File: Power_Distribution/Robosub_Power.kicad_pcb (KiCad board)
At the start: 2 copper layers, 120 x 60 mm, 47 parts, among them J1 1135333, J10 1135333, J14 Conn_01x04, J2 1135333, J3 1135333, J4 1135333, J5 1135333, J6 1135333, J7 1135333, J8 1135333, J9 1135333, U1 INA300AIDSQT, U2 SN74LVC1G97DBVR, U3 AUIR3241STR, U4 BSC0702LSATMA1, U5 BSC0702LSATMA1, U6 BSC0702LSATMA1, U7 NVTR01P02LT1G, U8 NVTR01P02LT1G

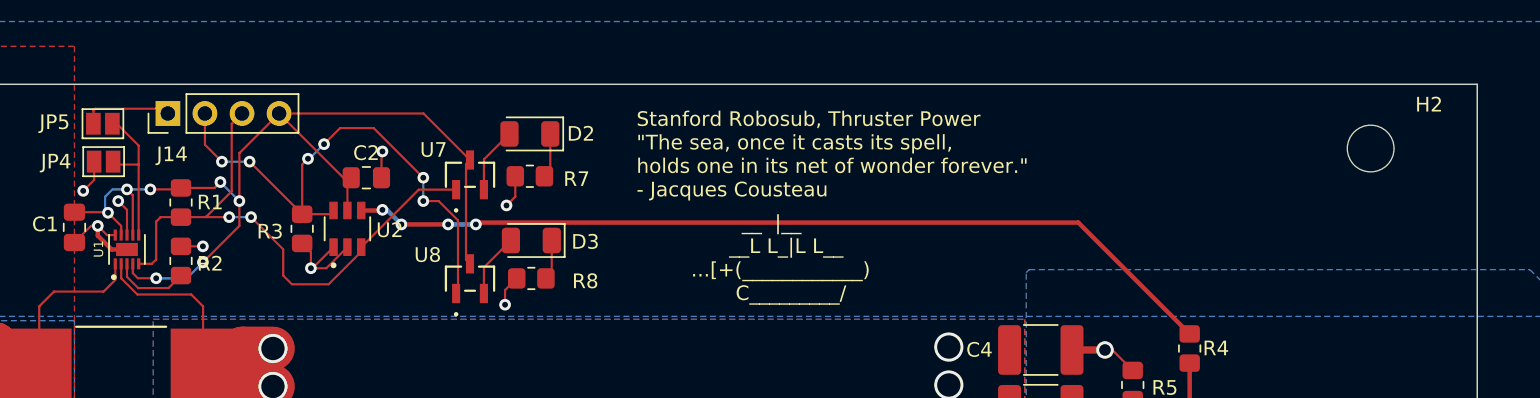
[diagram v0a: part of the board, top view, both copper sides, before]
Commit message: power rev2[fix diodes, ground loop, silkscreen]
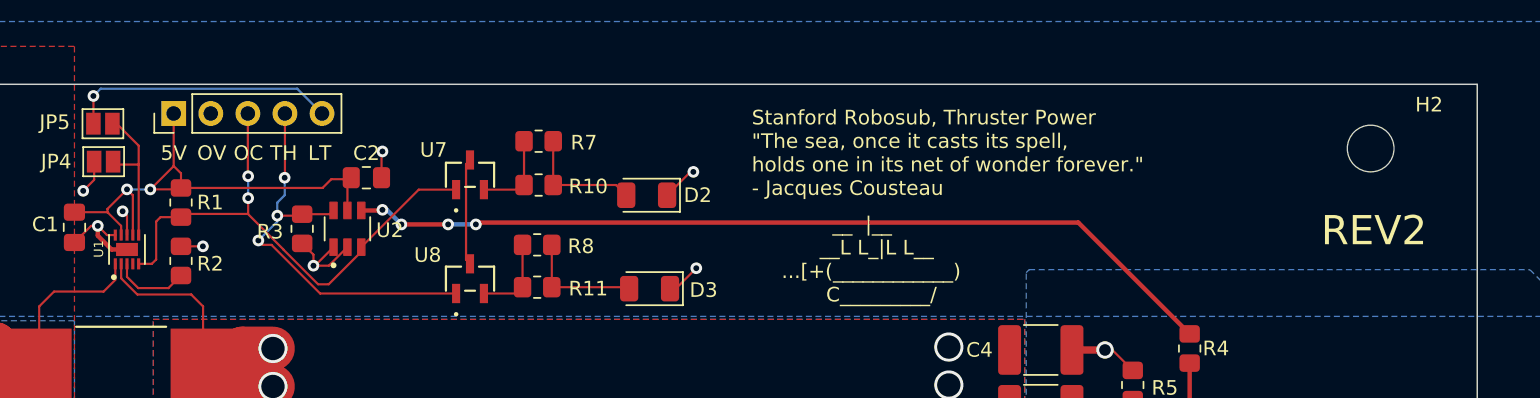
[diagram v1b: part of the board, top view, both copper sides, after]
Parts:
- removed J14: Conn_01x04, Connector_PinHeader_2.54mm:PinHeader_1x04_P2.54mm_Vertical
- added J11: Conn_01x05_Pin, Connector_PinHeader_2.54mm:PinHeader_1x05_P2.54mm_Vertical, F.Cu at (233.5, 135.6)
- added R10: 110, Resistor_SMD:R_0805_2012Metric_Pad1.20x1.40mm_HandSolder, F.Cu at (258.5, 140.5)
- added R11: 110, Resistor_SMD:R_0805_2012Metric_Pad1.20x1.40mm_HandSolder, F.Cu at (258.4, 147.5)
- R7, R8: value 100 -> 110
- moved D2 9.04 mm to (265.9, 141.2)
- moved D3 8.75 mm to (266.1, 147.6)
- moved R7 2.47 mm to (258.5, 137.5), turned to 180 degrees
- moved R8 2.33 mm to (258.4, 144.6), turned to 180 degrees
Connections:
- D2 pad 1: Net-(D2-K) -> GND
- D3 pad 1: Net-(D3-K) -> GND
- R7 pad 1: GND -> Net-(D2-A)
- R7 pad 2: Net-(D2-K) -> Net-(U7-SOURCE)
- R8 pad 1: GND -> Net-(D3-A)
- R8 pad 2: Net-(D3-K) -> Net-(U8-SOURCE)
- U7 pad 2: Net-(D2-A) -> Net-(U7-SOURCE)
- U8 pad 2: Net-(D3-A) -> Net-(U8-SOURCE)
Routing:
- net +5V: track 67.6 -> 41.9 mm, vias 7 -> 2
- net LATCH: track 5.73 -> 18.5 mm, vias 0 -> 1
- net THRUST_EN: track 36.6 -> 28.4 mm, vias 6 -> 3
- net Net-(U7-SOURCE): track 0.00 -> 5.88 mm
- net Net-(U8-SOURCE): track 0.00 -> 5.12 mm
- net Net-(D2-A): track 4.54 -> 8.29 mm
- net Net-(D3-A): track 4.40 -> 8.10 mm
- net Net-(D2-K): track 2.50 -> 0.00 mm
- net OCP_N: track 38.2 -> 35.8 mm
- net Net-(D3-K): track 2.20 -> 0.00 mm
- net GND: track 150.0 -> 148.6 mm
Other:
- board text added: "5V"
- board text added: "LT"
- board text added: "OC"
- board text added: "OV"
- board text added: "REV2"
- board text added: "TH"

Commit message: rev2[ready]
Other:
- board text added: "+BATT"
- board text added: "GND"
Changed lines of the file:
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@@
     (effects (font (size 1 1) (thickness 0.15)) (justify left bottom))
+  )
+  (gr_text "GND" (at 203.9 142.7) (layer "F.SilkS")
+    (effects (font (size 1.5 1.5) (thickness 0.3) bold) (justify left bottom))
   )
   (gr_text "NOSTUFF" (at 288.2 172.8) (layer "F.SilkS")
     (effects (font (size 1 1) (thickness 0.15)) (justify left bottom))
+  )
+  (gr_text "GND" (at 227.5 177.8) (layer "F.SilkS")
+    (effects (font (size 1.5 1.5) (thickness 0.3) bold) (justify left bottom))
+  )
+  (gr_text "+BATT" (at 230.55 175.75) (layer "F.SilkS")
+    (effects (font (size 1.5 1.5) (thickness 0.3) bold) (justify left bottom))
   )
   (gr_text "         __  |__\n       __L L_|L L__\n ...[+(____________)\n        C_________/" (at 274.7 148.6) (layer "F.SilkS")
@@
     (effects (font (size 1 1) (thickness 0.15)) (justify left bottom))
   )
+  (gr_text "+BATT" (at 203.8 169.3) (layer "F.SilkS")
+    (effects (font (size 1.5 1.5) (thickness 0.3) bold) (justify left bottom))
+  )
   (gr_text "OC" (at 237.6 138.9) (layer "F.SilkS")

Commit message: rev2 [final]
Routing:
- net LATCH: track 18.5 -> 19.3 mm, vias 1 -> 0
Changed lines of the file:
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@@
   (gr_rect (start 202.8 133.6) (end 322.8 193.6)
     (stroke (width 0.1) (type default)) (fill none) (layer "Edge.Cuts"))
-  (gr_text "REV2" (at 312.1 144.8) (layer "F.SilkS")
+  (gr_text "REV2" (at 310.9 157.55) (layer "F.SilkS")
     (effects (font (size 2 2) (thickness 0.15)) (justify left bottom))
   )
@@
   (via (at 286.6 165.7) (size 2) (drill 1.6) (layers "F.Cu" "B.Cu") (net 19))
   (via (at 286.6 154.2) (size 2) (drill 1.6) (layers "F.Cu" "B.Cu") (net 19))
+  (segment (start 243.6 134) (end 228.4 134) (width 0.15) (layer "F.Cu") (net 20))
+  (segment (start 228.4 134) (end 228 134.4) (width 0.15) (layer "F.Cu") (net 20))
   (segment (start 228 134.4) (end 228 136.3) (width 0.15) (layer "F.Cu") (net 20))
-  (via (at 228 134.4) (size 0.8) (drill 0.4) (layers "F.Cu" "B.Cu") (net 20))
-  (segment (start 228 134.4) (end 228.5 133.9) (width 0.15) (layer "B.Cu") (net 20))
-  (segment (start 241.96 133.9) (end 243.66 135.6) (width 0.15) (layer "B.Cu") (net 20))
-  (segment (start 228.5 133.9) (end 241.96 133.9) (width 0.15) (layer "B.Cu") (net 20))
+  (segment (start 243.66 134.06) (end 243.6 134) (width 0.15) (layer "F.Cu") (net 20))
+  (segment (start 243.66 135.6) (end 243.66 134.06) (width 0.15) (layer "F.Cu") (net 20))
   (segment (start 231.1 137.8) (end 231.1 139.1) (width 0.15) (layer "F.Cu") (net 21))
   (segment (start 229.6 136.3) (end 231.1 137.8) (width 0.15) (layer "F.Cu") (net 21))
